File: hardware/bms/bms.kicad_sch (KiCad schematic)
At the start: 39 parts

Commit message: Sch mostly complete! Just have the USB C connector left to sort out.
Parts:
- added R?: 56k, Resistor_SMD:R_0603_1608Metric, symbol Device:R_Small_US
- gave numbers to parts that had none: 17
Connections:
- net VUSB_5V: now also R?.2
- net at J11.A5 (CC): now also R?.1

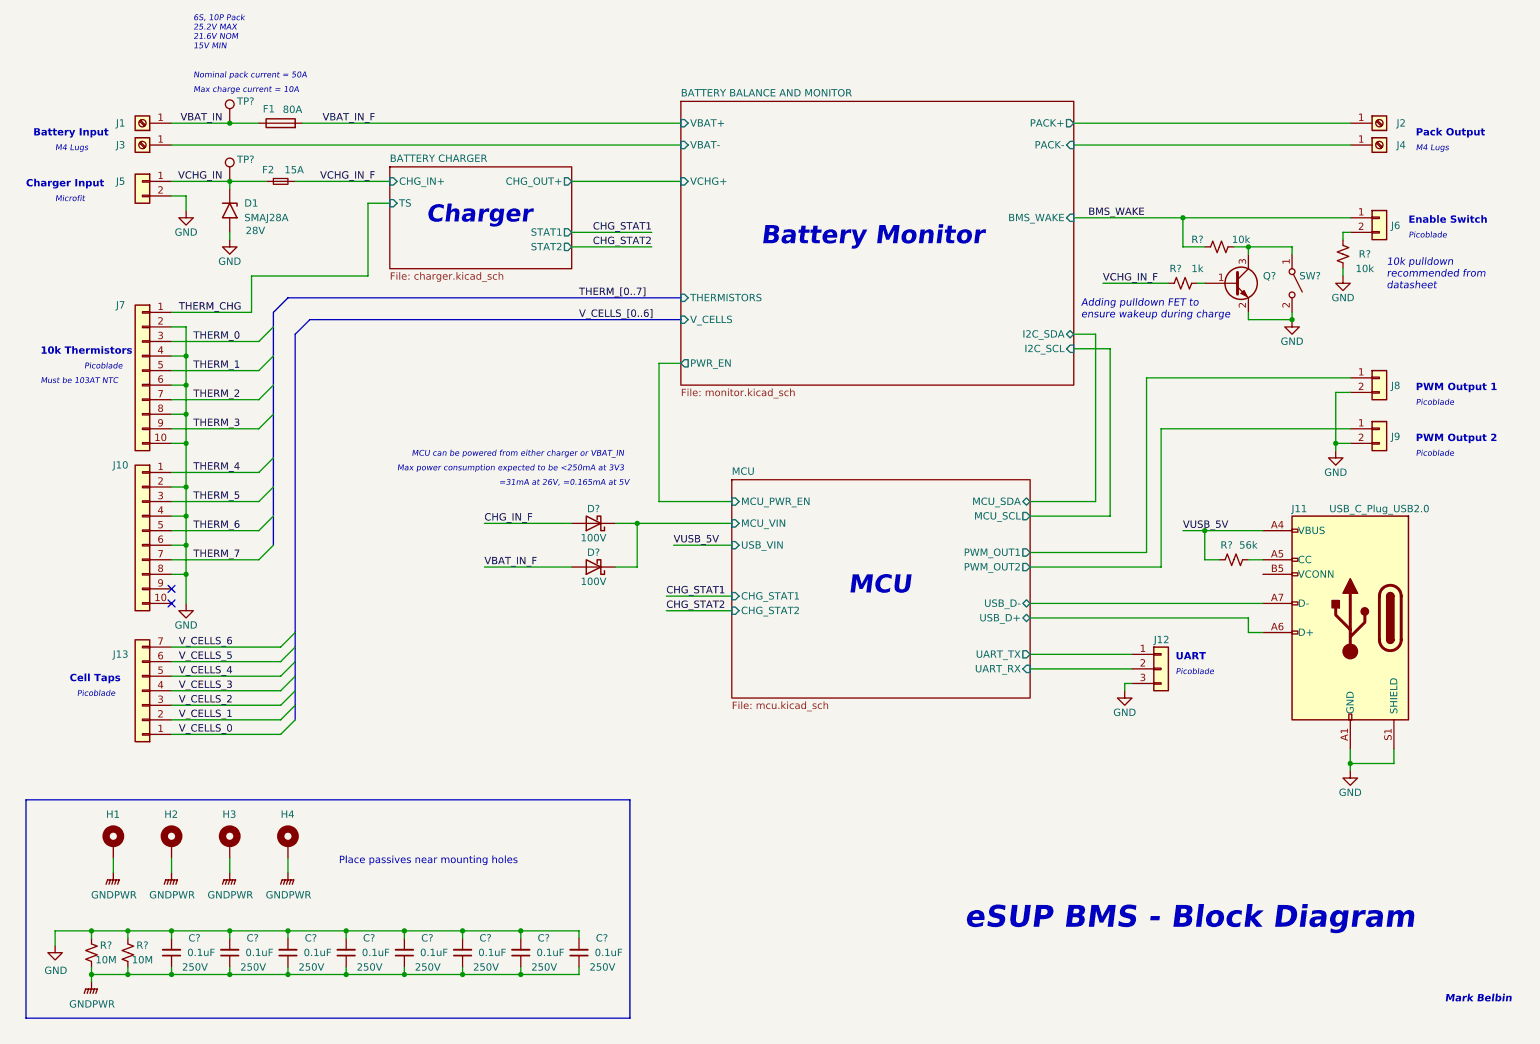
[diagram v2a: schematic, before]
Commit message: Updated USB C connector, fixed all sch ERC errors, imported footprints into pcb file, fixed any pcb import errors.
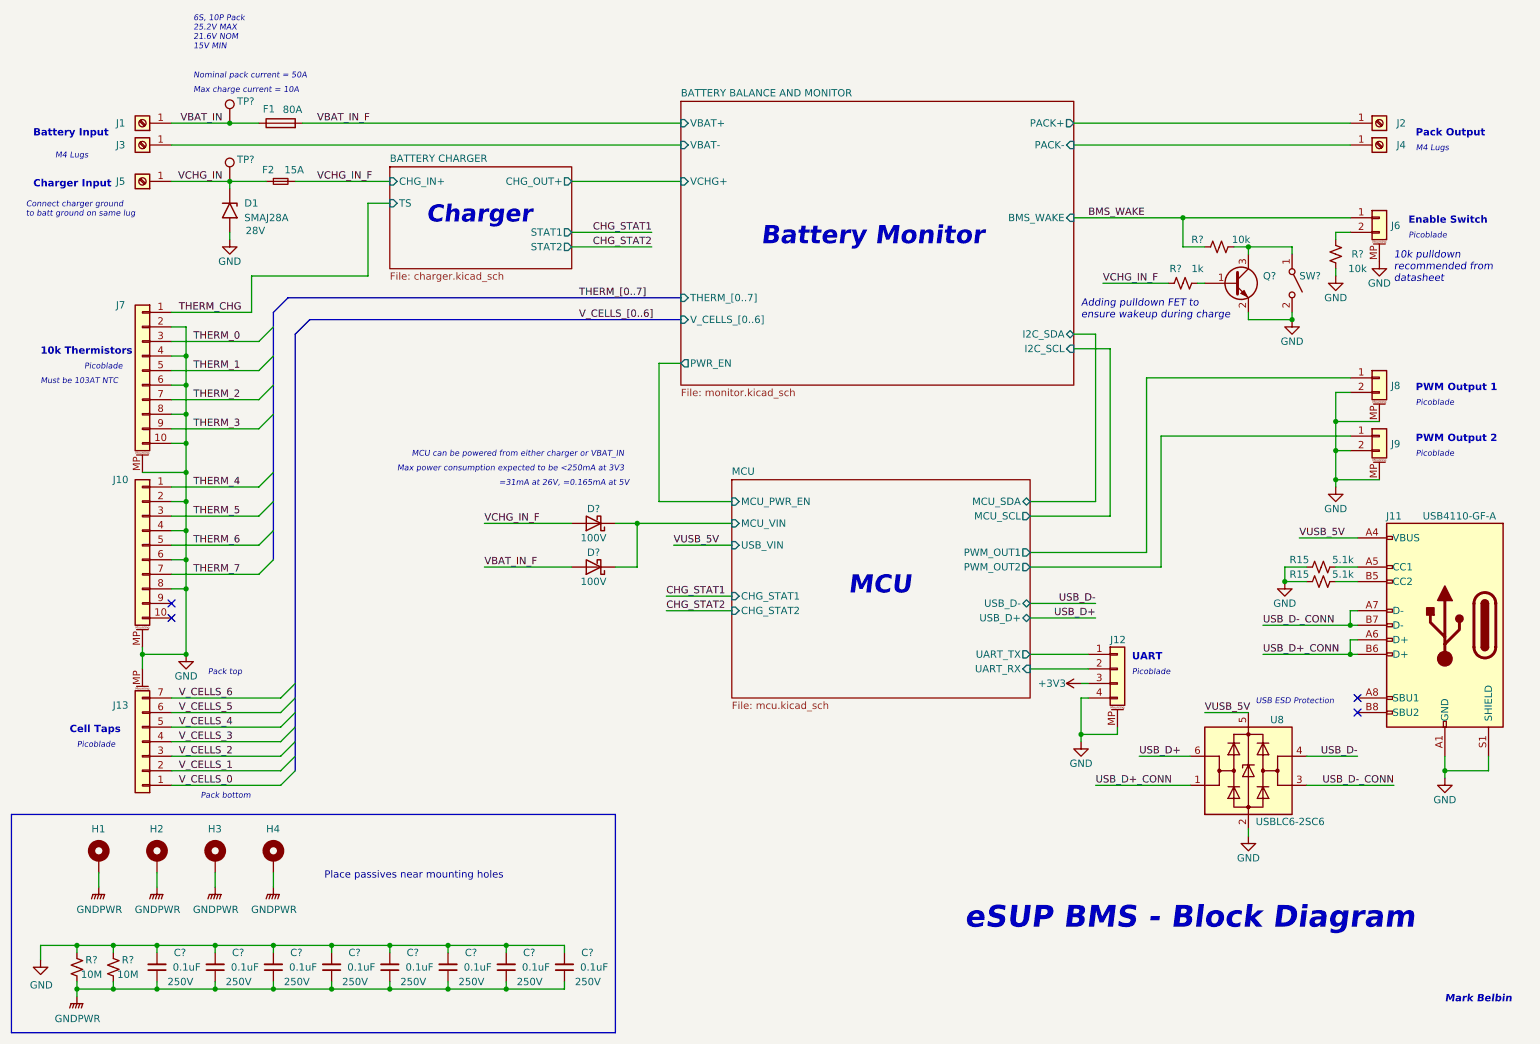
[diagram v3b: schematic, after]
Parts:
- removed J11: USB_C_Plug_USB2.0, symbol Connector:USB_C_Plug_USB2.0
- removed J5: Conn_01x02, bms:MOLEX_436500214, symbol Connector_Generic:Conn_01x02
- removed R?: 56k, Resistor_SMD:R_0603_1608Metric, symbol Device:R_Small_US
- added J11: USB_C_Receptacle_USB2.0, bms:USB_C_Receptacle_GCT_USB4110, symbol Connector:USB_C_Receptacle_USB2.0
- added J5: Screw_Terminal_01x01, bms:Wurth_746600430R, symbol Connector:Screw_Terminal_01x01
- added R15 (x2): 5.1k, Resistor_SMD:R_0603_1608Metric, symbol Device:R_Small_US
- added U8: USBLC6-2SC6, Package_TO_SOT_SMD:SOT-23-6, symbol Power_Protection:USBLC6-2SC6
- J10, J7: symbol Connector_Generic:Conn_01x10 -> Connector_Generic_MountingPin:Conn_01x10_MountingPin
- J12: footprint Connector_Molex:Molex_PicoBlade_53261-0371_1x03-1MP_P1.25mm_Horizontal -> Connector_Molex:Molex_PicoBlade_53261-0471_1x04-1MP_P1.25mm_Horizontal; symbol Connector_Generic:Conn_01x03 -> Connector_Generic_MountingPin:Conn_01x04_MountingPin; MFG PN 0532610371 -> 0532610471
- J13: symbol Connector_Generic:Conn_01x07 -> Connector_Generic_MountingPin:Conn_01x07_MountingPin
- J6, J8, J9: symbol Connector_Generic:Conn_01x02 -> Connector_Generic_MountingPin:Conn_01x02_MountingPin
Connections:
- net CHG_IN_F is gone; now on net VCHG_IN_F: D?.2 (A)
- net GND: now also J10.MP (MountPin), J12.4 (Pin_4), J12.MP (MountPin), J13.MP (MountPin), J6.MP (MountPin), J7.MP (MountPin), J8.MP (MountPin), J9.MP (MountPin), J11.A1 (GND), J11.A12 (GND), J11.B1 (GND), J11.B12 (GND), J11.S1 (SHIELD), R15.1, R15.1, U8.2 (GND); no longer J12.3 (Pin_3)
- net VCHG_IN: now also J5.1 (Pin_1)
- net VUSB_5V: now also J11.A4 (VBUS), J11.A9 (VBUS), J11.B4 (VBUS), J11.B9 (VBUS), U8.5 (VBUS)
- new net: J11.B5 (CC2), R15.2
- new net: J11.A5 (CC1), R15.2
- new net +3V3: J12.3 (Pin_3)
- new net USB_D+: U8.6 (I/O1)
- new net USB_D+_CONN: J11.A6 (D+), J11.B6 (D+), U8.1 (I/O1)
- new net USB_D-: U8.4 (I/O2)
- new net USB_D-_CONN: J11.A7 (D-), J11.B7 (D-), U8.3 (I/O2)
- no-connect marks 2 -> 4
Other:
- sheet BATTERY BALANCE AND MONITOR ports: added THERM_[0..7], V_CELLS_[0..6]; removed THERMISTORS, V_CELLS
- note added: "Connect charger ground to batt ground on same lug"
- note added: "Pack bottom"
- note added: "Pack top"
- note added: "USB ESD Protection"
- note removed: "Microfit"
- moved on the sheet: C?, H1, H2, H3, H4, R?

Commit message: Sch cleanup, added extra netties
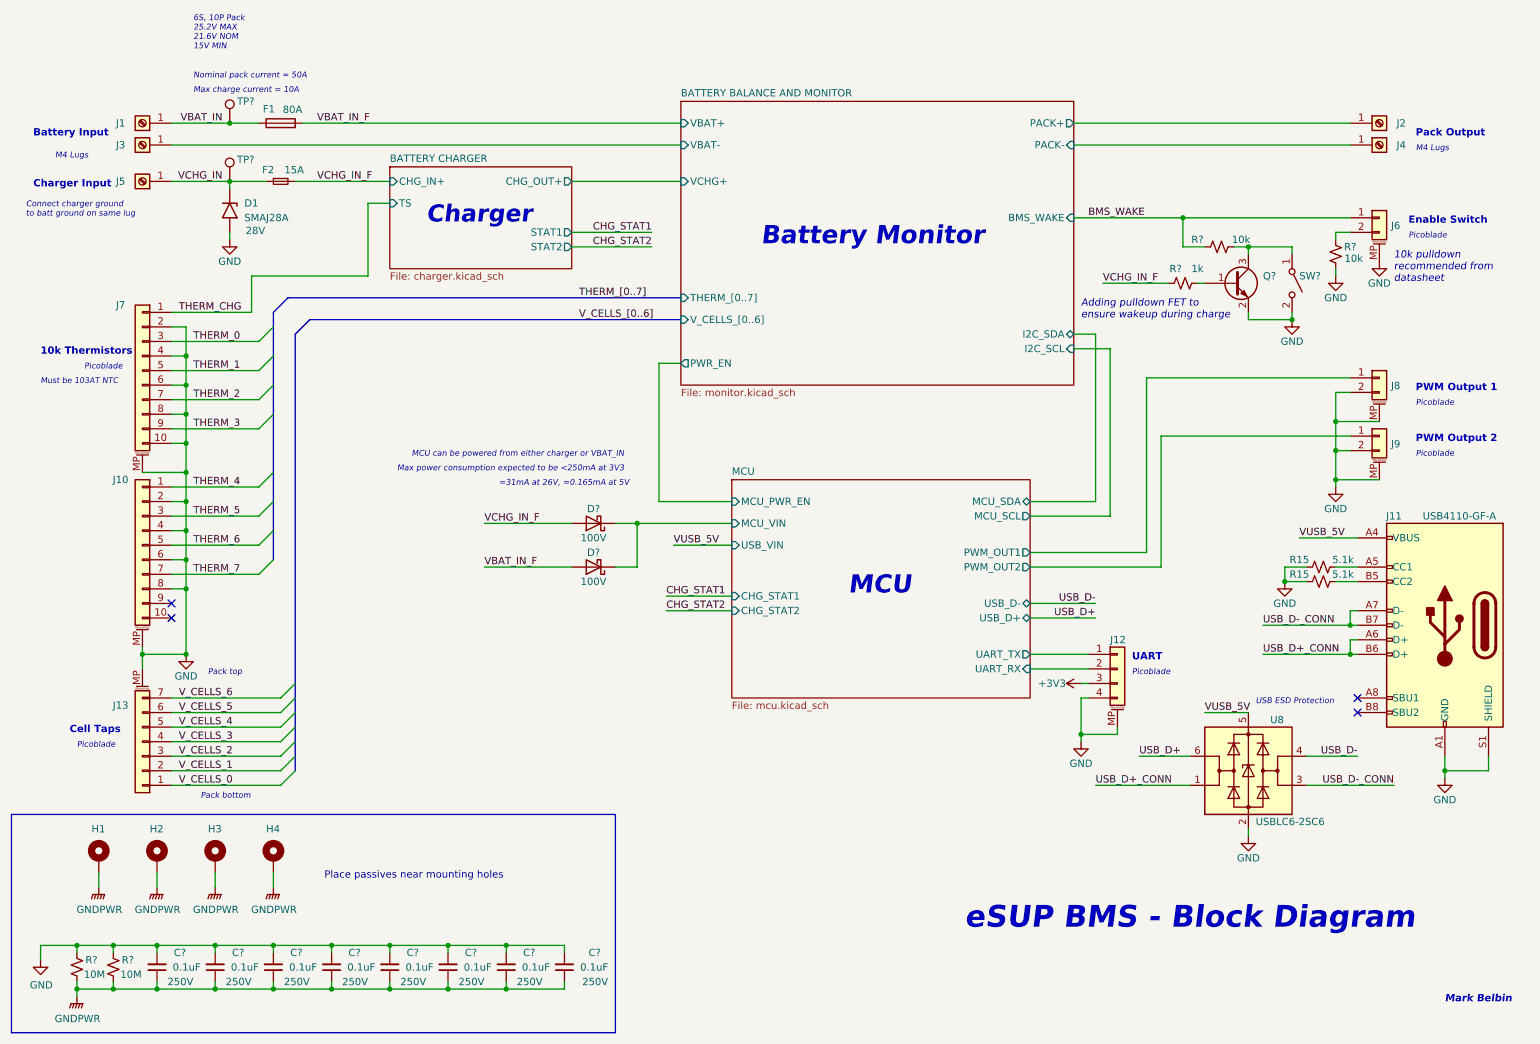
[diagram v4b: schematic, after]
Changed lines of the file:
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@@
       (effects (font (size 1.27 1.27)))
     )
-    (property "Value" "10M" (at 30.48 185.42 0)
+    (property "Value" "10M" (at 31.0043 185.4125 0)
       (effects (font (size 1.27 1.27)))
     )
@@
       (effects (font (size 1.27 1.27)))
     )
-    (property "Value" "10M" (at 36.83 185.42 0)
+    (property "Value" "10M" (at 37.3841 185.4125 0)
       (effects (font (size 1.27 1.27)))
     )
@@
   (symbol (lib_id "Device:C_Small") (at 113.03 184.15 180) (unit 1)
     (in_bom yes) (on_board yes) (dnp no)
-    (property "Reference" "C?" (at 118.11 181.61 0)
+    (property "Reference" "C?" (at 119.38 181.61 0)
       (effects (font (size 1.27 1.27)) (justify left))
     )
@@
       (effects (font (size 1.27 1.27)) hide)
     )
-    (property "Voltage" "250V" (at 119.38 186.69 0)
+    (property "Voltage" "250V" (at 120.65 186.69 0)
       (effects (font (size 1.27 1.27)) (justify left))
     )
@@
   (symbol (lib_id "Device:R_Small_US") (at 247.65 59.69 0) (unit 1)
     (in_bom yes) (on_board yes) (dnp no)
-    (property "Reference" "R?" (at 251.46 59.69 0)
-      (effects (font (size 1.27 1.27)))
-    )
-    (property "Value" "10k" (at 251.46 62.23 0)
-      (effects (font (size 1.27 1.27)))
-    )
+    (property "Reference" "R?" (at 250.19 58.42 0)
+      (effects (font (size 1.27 1.27)))
+    )
+    (property "Value" "10k" (at 250.7959 60.443 0)
+      (effects (font (size 1.27 1.27)))
+    )

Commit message: Continued layout, defined board area based on mech assembly
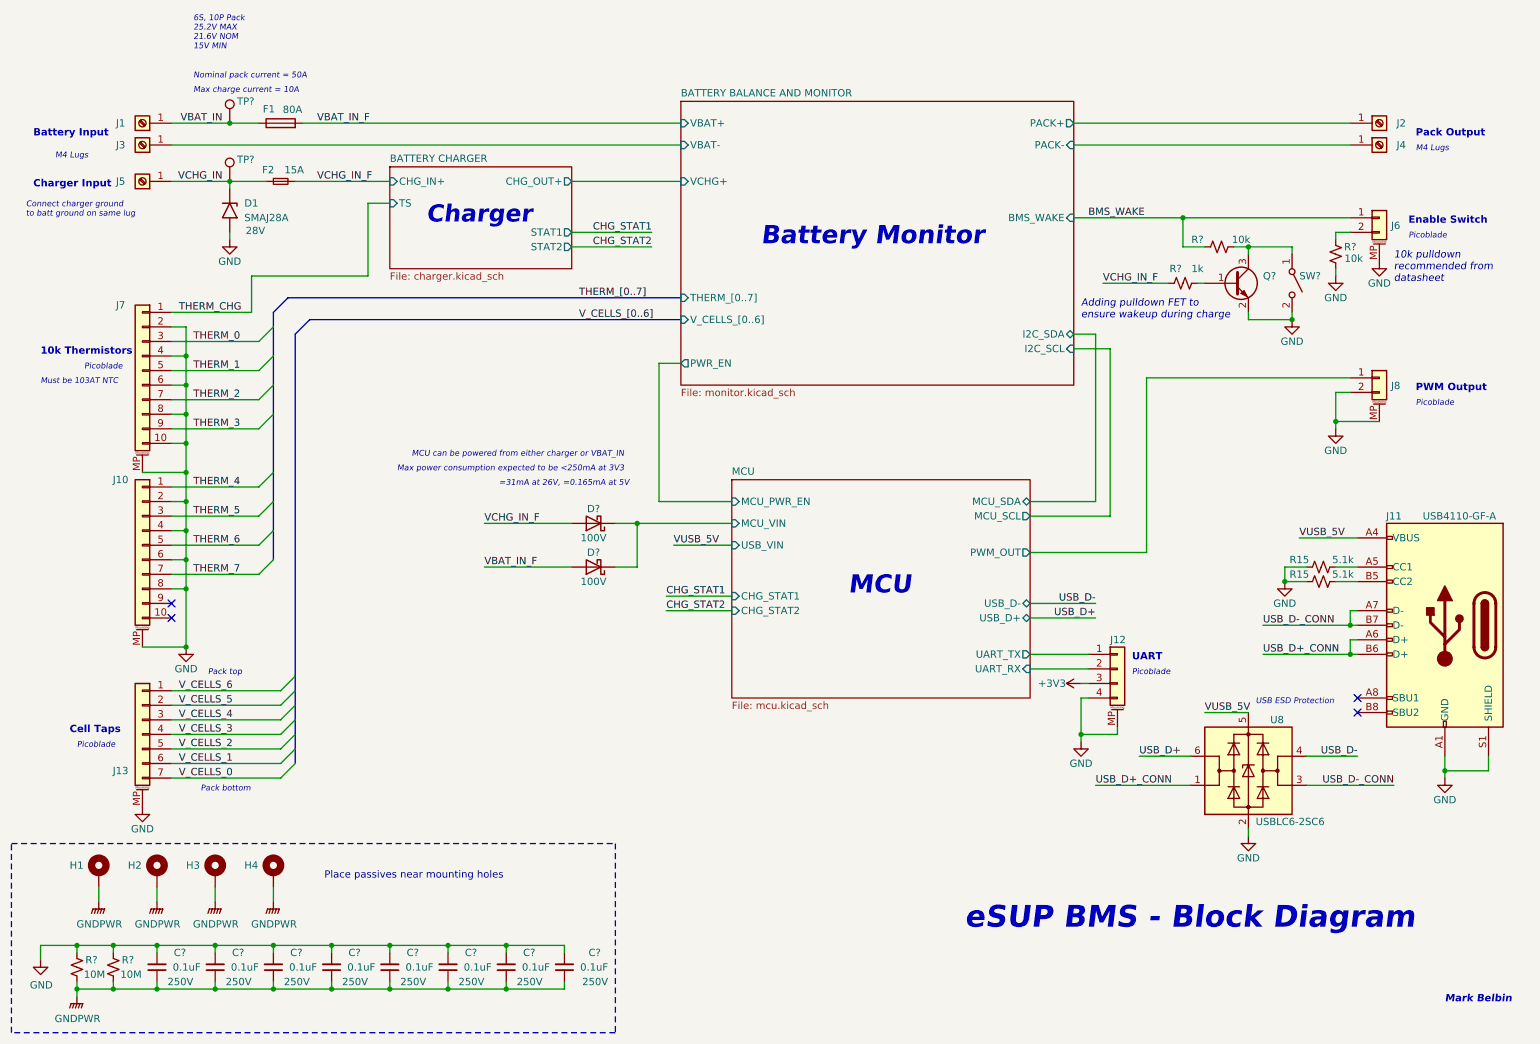
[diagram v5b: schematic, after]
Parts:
- removed J9: Conn_01x02, Connector_Molex:Molex_PicoBlade_53261-0271_1x02-1MP_P1.25mm_Horizontal, symbol Connector_Generic_MountingPin:Conn_01x02_MountingPin
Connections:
- net V_CELLS_0: now also J13.7 (Pin_7); no longer J13.1 (Pin_1)
- net V_CELLS_1: now also J13.6 (Pin_6); no longer J13.2 (Pin_2)
- net V_CELLS_2: now also J13.5 (Pin_5); no longer J13.3 (Pin_3)
- net V_CELLS_4: now also J13.3 (Pin_3); no longer J13.5 (Pin_5)
- net V_CELLS_5: now also J13.2 (Pin_2); no longer J13.6 (Pin_6)
- net V_CELLS_6: now also J13.1 (Pin_1); no longer J13.7 (Pin_7)
- net MCU/PWM_OUT1 renamed MCU/PWM_OUT
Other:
- sheet MCU ports: added PWM_OUT; removed PWM_OUT1, PWM_OUT2
- note added: "PWM Output"
- note removed: "PWM Output 1"
- note removed: "PWM Output 2"
- moved on the sheet: H1, H2, H3, H4, J13

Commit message: Updated test points to 0.5mm to save space, continued layout
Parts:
- TP? (x2): footprint TestPoint:TestPoint_Pad_D1.0mm -> bms:TestPoint_Pad_D0.5mm; now left out of the parts list
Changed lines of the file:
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@@
   )
   (symbol (lib_id "Connector:TestPoint") (at 54.61 36.83 0) (unit 1)
-    (in_bom yes) (on_board yes) (dnp no)
+    (in_bom no) (on_board yes) (dnp no)
     (property "Reference" "TP?" (at 55.88 33.02 0)
       (effects (font (size 1.27 1.27)) (justify left))
@@
       (effects (font (size 1.27 1.27)) (justify left) hide)
     )
-    (property "Footprint" "TestPoint:TestPoint_Pad_D1.0mm" (at 59.69 36.83 0)
+    (property "Footprint" "bms:TestPoint_Pad_D0.5mm" (at 59.69 36.83 0)
       (effects (font (size 1.27 1.27)) hide)
     )
@@
   )
   (symbol (lib_id "Connector:TestPoint") (at 54.61 46.99 0) (unit 1)
-    (in_bom yes) (on_board yes) (dnp no)
+    (in_bom no) (on_board yes) (dnp no)
     (property "Reference" "TP?" (at 55.88 43.18 0)
       (effects (font (size 1.27 1.27)) (justify left))
@@
       (effects (font (size 1.27 1.27)) (justify left) hide)
     )
-    (property "Footprint" "TestPoint:TestPoint_Pad_D1.0mm" (at 59.69 46.99 0)
-      (effects (font (size 1.27 1.27)) hide)
-    )
+    (property "Footprint" "bms:TestPoint_Pad_D0.5mm" (at 59.69 46.99 0)
+      (effects (font (size 1.27 1.27)) hide)
+    )
